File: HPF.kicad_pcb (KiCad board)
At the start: 4 copper layers, 100 x 100 mm, 174 parts, among them J1 CONN_COAXIAL, J2 Conn_01x12, J3 CONN_COAXIAL, J4 CONN_COAXIAL, J5 CONN_COAXIAL, Q2 zvp2106G, U1 AP1117-50, U2 PGA103+

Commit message: new stitching, new gerber
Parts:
- added REF**: via, via:via, F.Cu at (165.0, 111.0)
- added REF**: via, via:via, F.Cu at (156.0, 111.0)
- added REF**: via, via:via, F.Cu at (162.0, 108.0)
- added REF**: via, via:via, F.Cu at (161.0, 108.0)
- added REF**: via, via:via, F.Cu at (160.0, 108.0)
- added REF**: via, via:via, F.Cu at (159.0, 108.0)
- added REF**: via, via:via, F.Cu at (158.0, 108.0)
- added REF**: via, via:via, F.Cu at (157.0, 108.0)
- added REF**: via, via:via, F.Cu at (156.0, 108.0)
- added REF**: via, via:via, F.Cu at (155.0, 108.0)
- added REF**: via, via:via, F.Cu at (154.0, 108.0)
- added REF**: via, via:via, F.Cu at (153.0, 108.0)
- added REF**: via, via:via, F.Cu at (155.0, 111.0)
- added REF**: via, via:via, F.Cu at (152.0, 108.0)
- added REF**: via, via:via, F.Cu at (151.0, 108.0)
- added REF**: via, via:via, F.Cu at (150.0, 108.0)
- added REF**: via, via:via, F.Cu at (149.0, 108.0)
- added REF**: via, via:via, F.Cu at (148.0, 108.0)
- added REF**: via, via:via, F.Cu at (147.0, 108.0)
- added REF**: via, via:via, F.Cu at (146.0, 108.0)
- added REF**: via, via:via, F.Cu at (145.0, 108.0)
- added REF**: via, via:via, F.Cu at (144.0, 108.0)
- added REF**: via, via:via, F.Cu at (143.0, 108.0)
- added REF**: via, via:via, F.Cu at (154.0, 111.0)
- added REF**: via, via:via, F.Cu at (142.0, 108.0)
- added REF**: via, via:via, F.Cu at (141.0, 108.0)
- added REF**: via, via:via, F.Cu at (140.0, 108.0)
- added REF**: via, via:via, F.Cu at (139.0, 108.0)
- added REF**: via, via:via, F.Cu at (138.0, 108.0)
- added REF**: via, via:via, F.Cu at (137.0, 108.0)
- added REF**: via, via:via, F.Cu at (136.0, 108.0)
- added REF**: via, via:via, F.Cu at (135.0, 108.0)
- added REF**: via, via:via, F.Cu at (134.0, 108.0)
- added REF**: via, via:via, F.Cu at (165.0, 107.0)
- added REF**: via, via:via, F.Cu at (153.0, 111.0)
- added REF**: via, via:via, F.Cu at (164.0, 107.0)
- added REF**: via, via:via, F.Cu at (163.0, 107.0)
- added REF**: via, via:via, F.Cu at (162.0, 107.0)
- added REF**: via, via:via, F.Cu at (161.0, 107.0)
- added REF**: via, via:via, F.Cu at (160.0, 107.0)
- added REF**: via, via:via, F.Cu at (159.0, 107.0)
- added REF**: via, via:via, F.Cu at (158.0, 107.0)
- added REF**: via, via:via, F.Cu at (157.0, 107.0)
- added REF**: via, via:via, F.Cu at (156.0, 107.0)
- added REF**: via, via:via, F.Cu at (155.0, 107.0)
- added REF**: via, via:via, F.Cu at (152.0, 111.0)
- added REF**: via, via:via, F.Cu at (154.0, 107.0)
- added REF**: via, via:via, F.Cu at (153.0, 107.0)
- added REF**: via, via:via, F.Cu at (152.0, 107.0)
- added REF**: via, via:via, F.Cu at (151.0, 107.0)
- added REF**: via, via:via, F.Cu at (150.0, 107.0)
- added REF**: via, via:via, F.Cu at (149.0, 107.0)
- added REF**: via, via:via, F.Cu at (148.0, 107.0)
- added REF**: via, via:via, F.Cu at (147.0, 107.0)
- added REF**: via, via:via, F.Cu at (146.0, 107.0)
- added REF**: via, via:via, F.Cu at (145.0, 107.0)
- added REF**: via, via:via, F.Cu at (151.0, 111.0)
- added REF**: via, via:via, F.Cu at (144.0, 107.0)
- added REF**: via, via:via, F.Cu at (143.0, 107.0)
- added REF**: via, via:via, F.Cu at (142.0, 107.0)
- added REF**: via, via:via, F.Cu at (141.0, 107.0)
- added REF**: via, via:via, F.Cu at (140.0, 107.0)
- added REF**: via, via:via, F.Cu at (139.0, 107.0)
- added REF**: via, via:via, F.Cu at (138.0, 107.0)
- added REF**: via, via:via, F.Cu at (137.0, 107.0)
- added REF**: via, via:via, F.Cu at (136.0, 107.0)
- added REF**: via, via:via, F.Cu at (135.0, 107.0)
- added REF**: via, via:via, F.Cu at (150.0, 111.0)
- added REF**: via, via:via, F.Cu at (134.0, 107.0)
- added REF**: via, via:via, F.Cu at (189.0, 103.0)
- added REF**: via, via:via, F.Cu at (189.0, 102.0)
- added REF**: via, via:via, F.Cu at (189.0, 101.0)
- added REF**: via, via:via, F.Cu at (189.0, 100.0)
- added REF**: via, via:via, F.Cu at (189.0, 99.0)
- added REF**: via, via:via, F.Cu at (189.0, 98.0)
- added REF**: via, via:via, F.Cu at (189.0, 97.0)
- added REF**: via, via:via, F.Cu at (189.0, 96.0)
- added REF**: via, via:via, F.Cu at (189.0, 95.0)
- added REF**: via, via:via, F.Cu at (149.0, 111.0)
- added REF**: via, via:via, F.Cu at (189.0, 94.0)
- added REF**: via, via:via, F.Cu at (189.0, 93.0)
- added REF**: via, via:via, F.Cu at (189.0, 92.0)
- added REF**: via, via:via, F.Cu at (189.0, 91.0)
- added REF**: via, via:via, F.Cu at (189.0, 90.0)
- added REF**: via, via:via, F.Cu at (189.0, 89.0)
- added REF**: via, via:via, F.Cu at (189.0, 88.0)
- added REF**: via, via:via, F.Cu at (189.0, 87.0)
- added REF**: via, via:via, F.Cu at (189.0, 86.0)
- added REF**: via, via:via, F.Cu at (189.0, 85.0)
- added REF**: via, via:via, F.Cu at (148.0, 111.0)
- added REF**: via, via:via, F.Cu at (189.0, 84.0)
- added REF**: via, via:via, F.Cu at (189.0, 83.0)
- added REF**: via, via:via, F.Cu at (189.0, 82.0)
- added REF**: via, via:via, F.Cu at (189.0, 81.0)
- added REF**: via, via:via, F.Cu at (189.0, 80.0)
- added REF**: via, via:via, F.Cu at (189.0, 79.0)
- added REF**: via, via:via, F.Cu at (189.0, 78.0)
- added REF**: via, via:via, F.Cu at (189.0, 77.0)
- added REF**: via, via:via, F.Cu at (189.0, 76.0)
- added REF**: via, via:via, F.Cu at (189.0, 75.0)
- added REF**: via, via:via, F.Cu at (147.0, 111.0)
- added REF**: via, via:via, F.Cu at (189.0, 74.0)
- added REF**: via, via:via, F.Cu at (189.0, 73.0)
- added REF**: via, via:via, F.Cu at (189.0, 72.0)
- added REF**: via, via:via, F.Cu at (189.0, 71.0)
- added REF**: via, via:via, F.Cu at (189.0, 70.0)
- added REF**: via, via:via, F.Cu at (189.0, 69.0)
- added REF**: via, via:via, F.Cu at (189.0, 68.0)
- added REF**: via, via:via, F.Cu at (189.0, 67.0)
- added REF**: via, via:via, F.Cu at (189.0, 66.0)
- added REF**: via, via:via, F.Cu at (189.0, 65.0)
- added REF**: via, via:via, F.Cu at (164.0, 111.0)
- added REF**: via, via:via, F.Cu at (146.0, 111.0)
- added REF**: via, via:via, F.Cu at (189.0, 64.0)
- added REF**: via, via:via, F.Cu at (189.0, 63.0)
- added REF**: via, via:via, F.Cu at (189.0, 62.0)
- added REF**: via, via:via, F.Cu at (189.0, 61.0)
- added REF**: via, via:via, F.Cu at (189.0, 60.0)
- added REF**: via, via:via, F.Cu at (189.0, 59.0)
- added REF**: via, via:via, F.Cu at (189.0, 58.0)
- added REF**: via, via:via, F.Cu at (189.0, 57.0)
- added REF**: via, via:via, F.Cu at (189.0, 56.0)
- added REF**: via, via:via, F.Cu at (189.0, 55.0)
- added REF**: via, via:via, F.Cu at (145.0, 111.0)
- added REF**: via, via:via, F.Cu at (189.0, 54.0)
- added REF**: via, via:via, F.Cu at (189.0, 53.0)
- added REF**: via, via:via, F.Cu at (189.0, 52.0)
- added REF**: via, via:via, F.Cu at (189.0, 51.0)
- added REF**: via, via:via, F.Cu at (189.0, 50.0)
- added REF**: via, via:via, F.Cu at (189.0, 49.0)
- added REF**: via, via:via, F.Cu at (189.0, 48.0)
- added REF**: via, via:via, F.Cu at (189.0, 47.0)
- added REF**: via, via:via, F.Cu at (189.0, 46.0)
- added REF**: via, via:via, F.Cu at (189.0, 45.0)
- added REF**: via, via:via, F.Cu at (144.0, 111.0)
- added REF**: via, via:via, F.Cu at (189.0, 44.0)
- added REF**: via, via:via, F.Cu at (189.0, 43.0)
- added REF**: via, via:via, F.Cu at (189.0, 42.0)
- added REF**: via, via:via, F.Cu at (189.0, 41.0)
- added REF**: via, via:via, F.Cu at (189.0, 40.0)
- added REF**: via, via:via, F.Cu at (189.0, 39.0)
- added REF**: via, via:via, F.Cu at (189.0, 38.0)
- added REF**: via, via:via, F.Cu at (189.0, 37.0)
- added REF**: via, via:via, F.Cu at (189.0, 36.0)
- added REF**: via, via:via, F.Cu at (189.0, 35.0)
- added REF**: via, via:via, F.Cu at (143.0, 111.0)
- added REF**: via, via:via, F.Cu at (189.0, 34.0)
- added REF**: via, via:via, F.Cu at (189.0, 33.0)
- added REF**: via, via:via, F.Cu at (189.0, 32.0)
- added REF**: via, via:via, F.Cu at (189.0, 31.0)
- added REF**: via, via:via, F.Cu at (189.0, 30.0)
- added REF**: via, via:via, F.Cu at (189.0, 29.0)
- added REF**: via, via:via, F.Cu at (189.0, 28.0)
- added REF**: via, via:via, F.Cu at (189.0, 27.0)
- added REF**: via, via:via, F.Cu at (189.0, 26.0)
- added REF**: via, via:via, F.Cu at (189.0, 25.0)
- added REF**: via, via:via, F.Cu at (142.0, 111.0)
- added REF**: via, via:via, F.Cu at (189.0, 24.0)
- added REF**: via, via:via, F.Cu at (189.0, 23.0)
- added REF**: via, via:via, F.Cu at (189.0, 22.0)
- added REF**: via, via:via, F.Cu at (189.0, 21.0)
- added REF**: via, via:via, F.Cu at (181.0, 14.0)
- added REF**: via, via:via, F.Cu at (180.0, 14.0)
- added REF**: via, via:via, F.Cu at (179.0, 14.0)
- added REF**: via, via:via, F.Cu at (178.0, 14.0)
- added REF**: via, via:via, F.Cu at (177.0, 14.0)
- added REF**: via, via:via, F.Cu at (176.0, 14.0)
- added REF**: via, via:via, F.Cu at (141.0, 111.0)
- added REF**: via, via:via, F.Cu at (175.0, 14.0)
- added REF**: via, via:via, F.Cu at (174.0, 14.0)
- added REF**: via, via:via, F.Cu at (173.0, 14.0)
- added REF**: via, via:via, F.Cu at (172.0, 14.0)
- added REF**: via, via:via, F.Cu at (171.0, 14.0)
- added REF**: via, via:via, F.Cu at (170.0, 14.0)
- added REF**: via, via:via, F.Cu at (169.0, 14.0)
- added REF**: via, via:via, F.Cu at (168.0, 14.0)
- added REF**: via, via:via, F.Cu at (167.0, 14.0)
- added REF**: via, via:via, F.Cu at (166.0, 14.0)
- added REF**: via, via:via, F.Cu at (140.0, 111.0)
- added REF**: via, via:via, F.Cu at (165.0, 14.0)
- added REF**: via, via:via, F.Cu at (164.0, 14.0)
- added REF**: via, via:via, F.Cu at (163.0, 14.0)
- added REF**: via, via:via, F.Cu at (162.0, 14.0)
- added REF**: via, via:via, F.Cu at (161.0, 14.0)
- added REF**: via, via:via, F.Cu at (160.0, 14.0)
- added REF**: via, via:via, F.Cu at (159.0, 14.0)
- added REF**: via, via:via, F.Cu at (158.0, 14.0)
- added REF**: via, via:via, F.Cu at (157.0, 14.0)
- added REF**: via, via:via, F.Cu at (156.0, 14.0)
- added REF**: via, via:via, F.Cu at (139.0, 111.0)
- added REF**: via, via:via, F.Cu at (155.0, 14.0)
- added REF**: via, via:via, F.Cu at (154.0, 14.0)
- added REF**: via, via:via, F.Cu at (153.0, 14.0)
- added REF**: via, via:via, F.Cu at (152.0, 14.0)
- added REF**: via, via:via, F.Cu at (151.0, 14.0)
- added REF**: via, via:via, F.Cu at (150.0, 14.0)
- added REF**: via, via:via, F.Cu at (149.0, 14.0)
- added REF**: via, via:via, F.Cu at (148.0, 14.0)
- added REF**: via, via:via, F.Cu at (147.0, 14.0)
- added REF**: via, via:via, F.Cu at (146.0, 14.0)
- added REF**: via, via:via, F.Cu at (138.0, 111.0)
- added REF**: via, via:via, F.Cu at (145.0, 14.0)
- added REF**: via, via:via, F.Cu at (144.0, 14.0)
- added REF**: via, via:via, F.Cu at (143.0, 14.0)
- added REF**: via, via:via, F.Cu at (142.0, 14.0)
- added REF**: via, via:via, F.Cu at (141.0, 14.0)
- added REF**: via, via:via, F.Cu at (140.0, 14.0)
- added REF**: via, via:via, F.Cu at (139.0, 14.0)
- added REF**: via, via:via, F.Cu at (138.0, 14.0)
- added REF**: via, via:via, F.Cu at (137.0, 14.0)
- added REF**: via, via:via, F.Cu at (136.0, 14.0)
- added REF**: via, via:via, F.Cu at (137.0, 111.0)
- added REF**: via, via:via, F.Cu at (135.0, 14.0)
- added REF**: via, via:via, F.Cu at (134.0, 14.0)
- added REF**: via, via:via, F.Cu at (133.0, 14.0)
- added REF**: via, via:via, F.Cu at (132.0, 14.0)
- added REF**: via, via:via, F.Cu at (131.0, 14.0)
- added REF**: via, via:via, F.Cu at (130.0, 14.0)
- added REF**: via, via:via, F.Cu at (129.0, 14.0)
- added REF**: via, via:via, F.Cu at (128.0, 14.0)
- added REF**: via, via:via, F.Cu at (127.0, 14.0)
- added REF**: via, via:via, F.Cu at (126.0, 14.0)
- added REF**: via, via:via, F.Cu at (163.0, 111.0)
- added REF**: via, via:via, F.Cu at (136.0, 111.0)
- added REF**: via, via:via, F.Cu at (125.0, 14.0)
- added REF**: via, via:via, F.Cu at (124.0, 14.0)
- added REF**: via, via:via, F.Cu at (123.0, 14.0)
- added REF**: via, via:via, F.Cu at (122.0, 14.0)
- added REF**: via, via:via, F.Cu at (121.0, 14.0)
- added REF**: via, via:via, F.Cu at (120.0, 14.0)
- added REF**: via, via:via, F.Cu at (119.0, 14.0)
- added REF**: via, via:via, F.Cu at (118.0, 14.0)
- added REF**: via, via:via, F.Cu at (117.0, 14.0)
- added REF**: via, via:via, F.Cu at (116.0, 14.0)
- added REF**: via, via:via, F.Cu at (135.0, 111.0)
- added REF**: via, via:via, F.Cu at (115.0, 14.0)
- added REF**: via, via:via, F.Cu at (114.0, 14.0)
- added REF**: via, via:via, F.Cu at (113.0, 14.0)
- added REF**: via, via:via, F.Cu at (112.0, 14.0)
- added REF**: via, via:via, F.Cu at (111.0, 14.0)
- added REF**: via, via:via, F.Cu at (110.0, 14.0)
- added REF**: via, via:via, F.Cu at (109.0, 14.0)
- added REF**: via, via:via, F.Cu at (108.0, 14.0)
- added REF**: via, via:via, F.Cu at (107.0, 14.0)
- added REF**: via, via:via, F.Cu at (106.0, 14.0)
- added REF**: via, via:via, F.Cu at (134.0, 111.0)
- added REF**: via, via:via, F.Cu at (105.0, 14.0)
- added REF**: via, via:via, F.Cu at (104.0, 14.0)
- added REF**: via, via:via, F.Cu at (103.0, 14.0)
- added REF**: via, via:via, F.Cu at (102.0, 14.0)
- added REF**: via, via:via, F.Cu at (101.0, 14.0)
- added REF**: via, via:via, F.Cu at (100.0, 14.0)
- added REF**: via, via:via, F.Cu at (94.0, 103.0)
- added REF**: via, via:via, F.Cu at (93.0, 103.0)
- added REF**: via, via:via, F.Cu at (92.0, 103.0)
- added REF**: via, via:via, F.Cu at (91.0, 103.0)
- added REF**: via, via:via, F.Cu at (165.0, 110.0)
- added REF**: via, via:via, F.Cu at (94.0, 102.0)
- added REF**: via, via:via, F.Cu at (93.0, 102.0)
- added REF**: via, via:via, F.Cu at (92.0, 102.0)
- added REF**: via, via:via, F.Cu at (91.0, 102.0)
- added REF**: via, via:via, F.Cu at (94.0, 101.0)
- added REF**: via, via:via, F.Cu at (93.0, 101.0)
- added REF**: via, via:via, F.Cu at (92.0, 101.0)
- added REF**: via, via:via, F.Cu at (91.0, 101.0)
- added REF**: via, via:via, F.Cu at (94.0, 100.0)
- added REF**: via, via:via, F.Cu at (93.0, 100.0)
- added REF**: via, via:via, F.Cu at (164.0, 110.0)
- added REF**: via, via:via, F.Cu at (92.0, 100.0)
- added REF**: via, via:via, F.Cu at (91.0, 100.0)
- added REF**: via, via:via, F.Cu at (94.0, 99.0)
- added REF**: via, via:via, F.Cu at (93.0, 99.0)
- added REF**: via, via:via, F.Cu at (92.0, 99.0)
- added REF**: via, via:via, F.Cu at (91.0, 99.0)
- added REF**: via, via:via, F.Cu at (94.0, 98.0)
- added REF**: via, via:via, F.Cu at (93.0, 98.0)
- added REF**: via, via:via, F.Cu at (92.0, 98.0)
- added REF**: via, via:via, F.Cu at (91.0, 98.0)
- added REF**: via, via:via, F.Cu at (163.0, 110.0)
- added REF**: via, via:via, F.Cu at (94.0, 97.0)
- added REF**: via, via:via, F.Cu at (93.0, 97.0)
- added REF**: via, via:via, F.Cu at (92.0, 97.0)
- added REF**: via, via:via, F.Cu at (91.0, 97.0)
- added REF**: via, via:via, F.Cu at (94.0, 96.0)
- added REF**: via, via:via, F.Cu at (93.0, 96.0)
- added REF**: via, via:via, F.Cu at (92.0, 96.0)
- added REF**: via, via:via, F.Cu at (91.0, 96.0)
- added REF**: via, via:via, F.Cu at (94.0, 95.0)
- added REF**: via, via:via, F.Cu at (93.0, 95.0)
- added REF**: via, via:via, F.Cu at (162.0, 110.0)
- added REF**: via, via:via, F.Cu at (92.0, 95.0)
- added REF**: via, via:via, F.Cu at (91.0, 95.0)
- added REF**: via, via:via, F.Cu at (94.0, 94.0)
- added REF**: via, via:via, F.Cu at (93.0, 94.0)
- added REF**: via, via:via, F.Cu at (92.0, 94.0)
- added REF**: via, via:via, F.Cu at (91.0, 94.0)
- added REF**: via, via:via, F.Cu at (94.0, 93.0)
- added REF**: via, via:via, F.Cu at (93.0, 93.0)
- added REF**: via, via:via, F.Cu at (92.0, 93.0)
- added REF**: via, via:via, F.Cu at (91.0, 93.0)
- added REF**: via, via:via, F.Cu at (161.0, 110.0)
- added REF**: via, via:via, F.Cu at (94.0, 92.0)
- added REF**: via, via:via, F.Cu at (93.0, 92.0)
- added REF**: via, via:via, F.Cu at (92.0, 92.0)
- added REF**: via, via:via, F.Cu at (91.0, 92.0)
- added REF**: via, via:via, F.Cu at (94.0, 91.0)
- added REF**: via, via:via, F.Cu at (93.0, 91.0)
- added REF**: via, via:via, F.Cu at (92.0, 91.0)
- added REF**: via, via:via, F.Cu at (91.0, 91.0)
- added REF**: via, via:via, F.Cu at (94.0, 90.0)
- added REF**: via, via:via, F.Cu at (93.0, 90.0)
- added REF**: via, via:via, F.Cu at (160.0, 110.0)
- added REF**: via, via:via, F.Cu at (92.0, 90.0)
- added REF**: via, via:via, F.Cu at (91.0, 90.0)
- added REF**: via, via:via, F.Cu at (94.0, 89.0)
- added REF**: via, via:via, F.Cu at (93.0, 89.0)
- added REF**: via, via:via, F.Cu at (92.0, 89.0)
- added REF**: via, via:via, F.Cu at (91.0, 89.0)
- added REF**: via, via:via, F.Cu at (94.0, 88.0)
- added REF**: via, via:via, F.Cu at (93.0, 88.0)
- added REF**: via, via:via, F.Cu at (92.0, 88.0)
- added REF**: via, via:via, F.Cu at (91.0, 88.0)
- added REF**: via, via:via, F.Cu at (159.0, 110.0)
- added REF**: via, via:via, F.Cu at (94.0, 87.0)
- added REF**: via, via:via, F.Cu at (93.0, 87.0)
- added REF**: via, via:via, F.Cu at (92.0, 87.0)
- added REF**: via, via:via, F.Cu at (91.0, 87.0)
- added REF**: via, via:via, F.Cu at (94.0, 86.0)
- added REF**: via, via:via, F.Cu at (93.0, 86.0)
- added REF**: via, via:via, F.Cu at (92.0, 86.0)
- added REF**: via, via:via, F.Cu at (91.0, 86.0)
- added REF**: via, via:via, F.Cu at (94.0, 85.0)
- added REF**: via, via:via, F.Cu at (93.0, 85.0)
- added REF**: via, via:via, F.Cu at (162.0, 111.0)
- added REF**: via, via:via, F.Cu at (158.0, 110.0)
- added REF**: via, via:via, F.Cu at (92.0, 85.0)
- added REF**: via, via:via, F.Cu at (91.0, 85.0)
- added REF**: via, via:via, F.Cu at (94.0, 84.0)
- added REF**: via, via:via, F.Cu at (93.0, 84.0)
- added REF**: via, via:via, F.Cu at (92.0, 84.0)
- added REF**: via, via:via, F.Cu at (91.0, 84.0)
- added REF**: via, via:via, F.Cu at (94.0, 83.0)
- added REF**: via, via:via, F.Cu at (93.0, 83.0)
- added REF**: via, via:via, F.Cu at (92.0, 83.0)
- added REF**: via, via:via, F.Cu at (91.0, 83.0)
- added REF**: via, via:via, F.Cu at (157.0, 110.0)
- added REF**: via, via:via, F.Cu at (94.0, 82.0)
- added REF**: via, via:via, F.Cu at (93.0, 82.0)
- added REF**: via, via:via, F.Cu at (92.0, 82.0)
- added REF**: via, via:via, F.Cu at (91.0, 82.0)
- added REF**: via, via:via, F.Cu at (94.0, 81.0)
- added REF**: via, via:via, F.Cu at (93.0, 81.0)
- added REF**: via, via:via, F.Cu at (92.0, 81.0)
- added REF**: via, via:via, F.Cu at (91.0, 81.0)
- added REF**: via, via:via, F.Cu at (94.0, 80.0)
- added REF**: via, via:via, F.Cu at (93.0, 80.0)
- added REF**: via, via:via, F.Cu at (156.0, 110.0)
- added REF**: via, via:via, F.Cu at (92.0, 80.0)
- added REF**: via, via:via, F.Cu at (91.0, 80.0)
- added REF**: via, via:via, F.Cu at (94.0, 79.0)
- added REF**: via, via:via, F.Cu at (93.0, 79.0)
- added REF**: via, via:via, F.Cu at (92.0, 79.0)
- added REF**: via, via:via, F.Cu at (91.0, 79.0)
- added REF**: via, via:via, F.Cu at (94.0, 78.0)
- added REF**: via, via:via, F.Cu at (93.0, 78.0)
- added REF**: via, via:via, F.Cu at (92.0, 78.0)
- added REF**: via, via:via, F.Cu at (91.0, 78.0)
- added REF**: via, via:via, F.Cu at (155.0, 110.0)
- added REF**: via, via:via, F.Cu at (94.0, 77.0)
- added REF**: via, via:via, F.Cu at (93.0, 77.0)
- added REF**: via, via:via, F.Cu at (92.0, 77.0)
- added REF**: via, via:via, F.Cu at (91.0, 77.0)
- added REF**: via, via:via, F.Cu at (94.0, 76.0)
- added REF**: via, via:via, F.Cu at (93.0, 76.0)
- added REF**: via, via:via, F.Cu at (92.0, 76.0)
- added REF**: via, via:via, F.Cu at (91.0, 76.0)
- added REF**: via, via:via, F.Cu at (94.0, 75.0)
- added REF**: via, via:via, F.Cu at (93.0, 75.0)
- added REF**: via, via:via, F.Cu at (154.0, 110.0)
- added REF**: via, via:via, F.Cu at (92.0, 75.0)
- added REF**: via, via:via, F.Cu at (91.0, 75.0)
- added REF**: via, via:via, F.Cu at (94.0, 74.0)
- added REF**: via, via:via, F.Cu at (93.0, 74.0)
- added REF**: via, via:via, F.Cu at (92.0, 74.0)
- added REF**: via, via:via, F.Cu at (91.0, 74.0)
- added REF**: via, via:via, F.Cu at (94.0, 73.0)
- added REF**: via, via:via, F.Cu at (93.0, 73.0)
- added REF**: via, via:via, F.Cu at (92.0, 73.0)
- added REF**: via, via:via, F.Cu at (91.0, 73.0)
- added REF**: via, via:via, F.Cu at (153.0, 110.0)
- added REF**: via, via:via, F.Cu at (94.0, 72.0)
- added REF**: via, via:via, F.Cu at (93.0, 72.0)
- added REF**: via, via:via, F.Cu at (92.0, 72.0)
- added REF**: via, via:via, F.Cu at (91.0, 72.0)
- added REF**: via, via:via, F.Cu at (94.0, 71.0)
- added REF**: via, via:via, F.Cu at (93.0, 71.0)
- added REF**: via, via:via, F.Cu at (92.0, 71.0)
- added REF**: via, via:via, F.Cu at (91.0, 71.0)
- added REF**: via, via:via, F.Cu at (94.0, 70.0)
- added REF**: via, via:via, F.Cu at (93.0, 70.0)
- added REF**: via, via:via, F.Cu at (152.0, 110.0)
- added REF**: via, via:via, F.Cu at (92.0, 70.0)
- added REF**: via, via:via, F.Cu at (91.0, 70.0)
- added REF**: via, via:via, F.Cu at (94.0, 69.0)
- added REF**: via, via:via, F.Cu at (93.0, 69.0)
- added REF**: via, via:via, F.Cu at (92.0, 69.0)
- added REF**: via, via:via, F.Cu at (91.0, 69.0)
- added REF**: via, via:via, F.Cu at (94.0, 68.0)
- added REF**: via, via:via, F.Cu at (93.0, 68.0)
- added REF**: via, via:via, F.Cu at (92.0, 68.0)
- added REF**: via, via:via, F.Cu at (91.0, 68.0)
- added REF**: via, via:via, F.Cu at (151.0, 110.0)
- added REF**: via, via:via, F.Cu at (94.0, 67.0)
- added REF**: via, via:via, F.Cu at (93.0, 67.0)
- added REF**: via, via:via, F.Cu at (92.0, 67.0)
- added REF**: via, via:via, F.Cu at (91.0, 67.0)
- added REF**: via, via:via, F.Cu at (94.0, 66.0)
- added REF**: via, via:via, F.Cu at (93.0, 66.0)
- added REF**: via, via:via, F.Cu at (92.0, 66.0)
- added REF**: via, via:via, F.Cu at (91.0, 66.0)
- added REF**: via, via:via, F.Cu at (94.0, 65.0)
- added REF**: via, via:via, F.Cu at (93.0, 65.0)
- added REF**: via, via:via, F.Cu at (150.0, 110.0)
- added REF**: via, via:via, F.Cu at (92.0, 65.0)
- added REF**: via, via:via, F.Cu at (91.0, 65.0)
- added REF**: via, via:via, F.Cu at (94.0, 64.0)
- added REF**: via, via:via, F.Cu at (93.0, 64.0)
- added REF**: via, via:via, F.Cu at (92.0, 64.0)
- added REF**: via, via:via, F.Cu at (91.0, 64.0)
- added REF**: via, via:via, F.Cu at (94.0, 63.0)
- added REF**: via, via:via, F.Cu at (93.0, 63.0)
- added REF**: via, via:via, F.Cu at (92.0, 63.0)
- added REF**: via, via:via, F.Cu at (91.0, 63.0)
- added REF**: via, via:via, F.Cu at (149.0, 110.0)
- added REF**: via, via:via, F.Cu at (94.0, 62.0)
- added REF**: via, via:via, F.Cu at (93.0, 62.0)
- added REF**: via, via:via, F.Cu at (92.0, 62.0)
- added REF**: via, via:via, F.Cu at (91.0, 62.0)
- added REF**: via, via:via, F.Cu at (94.0, 61.0)
- added REF**: via, via:via, F.Cu at (93.0, 61.0)
- added REF**: via, via:via, F.Cu at (92.0, 61.0)
- added REF**: via, via:via, F.Cu at (91.0, 61.0)
- added REF**: via, via:via, F.Cu at (94.0, 60.0)
- added REF**: via, via:via, F.Cu at (93.0, 60.0)
- added REF**: via, via:via, F.Cu at (161.0, 111.0)
- added REF**: via, via:via, F.Cu at (148.0, 110.0)
- added REF**: via, via:via, F.Cu at (92.0, 60.0)
- added REF**: via, via:via, F.Cu at (91.0, 60.0)
- added REF**: via, via:via, F.Cu at (94.0, 59.0)
- added REF**: via, via:via, F.Cu at (93.0, 59.0)
- added REF**: via, via:via, F.Cu at (92.0, 59.0)
- added REF**: via, via:via, F.Cu at (91.0, 59.0)
- added REF**: via, via:via, F.Cu at (94.0, 58.0)
- added REF**: via, via:via, F.Cu at (93.0, 58.0)
- added REF**: via, via:via, F.Cu at (92.0, 58.0)
- added REF**: via, via:via, F.Cu at (91.0, 58.0)
- added REF**: via, via:via, F.Cu at (147.0, 110.0)
- added REF**: via, via:via, F.Cu at (94.0, 57.0)
- added REF**: via, via:via, F.Cu at (93.0, 57.0)
- added REF**: via, via:via, F.Cu at (92.0, 57.0)
- added REF**: via, via:via, F.Cu at (91.0, 57.0)
- added REF**: via, via:via, F.Cu at (94.0, 56.0)
- added REF**: via, via:via, F.Cu at (93.0, 56.0)
- added REF**: via, via:via, F.Cu at (92.0, 56.0)
- added REF**: via, via:via, F.Cu at (91.0, 56.0)
- added REF**: via, via:via, F.Cu at (94.0, 55.0)
- added REF**: via, via:via, F.Cu at (93.0, 55.0)
- added REF**: via, via:via, F.Cu at (146.0, 110.0)
- added REF**: via, via:via, F.Cu at (92.0, 55.0)
- added REF**: via, via:via, F.Cu at (91.0, 55.0)
- added REF**: via, via:via, F.Cu at (94.0, 54.0)
- added REF**: via, via:via, F.Cu at (93.0, 54.0)
- added REF**: via, via:via, F.Cu at (92.0, 54.0)
- added REF**: via, via:via, F.Cu at (91.0, 54.0)
- added REF**: via, via:via, F.Cu at (94.0, 53.0)
- added REF**: via, via:via, F.Cu at (93.0, 53.0)
- added REF**: via, via:via, F.Cu at (92.0, 53.0)
- added REF**: via, via:via, F.Cu at (91.0, 53.0)
- added REF**: via, via:via, F.Cu at (145.0, 110.0)
- added REF**: via, via:via, F.Cu at (94.0, 52.0)
- added REF**: via, via:via, F.Cu at (93.0, 52.0)
- added REF**: via, via:via, F.Cu at (92.0, 52.0)
- added REF**: via, via:via, F.Cu at (91.0, 52.0)
- added REF**: via, via:via, F.Cu at (94.0, 51.0)
- added REF**: via, via:via, F.Cu at (93.0, 51.0)
- added REF**: via, via:via, F.Cu at (92.0, 51.0)
- added REF**: via, via:via, F.Cu at (91.0, 51.0)
- added REF**: via, via:via, F.Cu at (94.0, 50.0)
- added REF**: via, via:via, F.Cu at (93.0, 50.0)
- added REF**: via, via:via, F.Cu at (144.0, 110.0)
- added REF**: via, via:via, F.Cu at (92.0, 50.0)
- added REF**: via, via:via, F.Cu at (91.0, 50.0)
- added REF**: via, via:via, F.Cu at (94.0, 49.0)
- added REF**: via, via:via, F.Cu at (93.0, 49.0)
- added REF**: via, via:via, F.Cu at (92.0, 49.0)
- added REF**: via, via:via, F.Cu at (91.0, 49.0)
- added REF**: via, via:via, F.Cu at (94.0, 48.0)
- added REF**: via, via:via, F.Cu at (93.0, 48.0)
- added REF**: via, via:via, F.Cu at (92.0, 48.0)
- added REF**: via, via:via, F.Cu at (91.0, 48.0)
- added REF**: via, via:via, F.Cu at (143.0, 110.0)
- added REF**: via, via:via, F.Cu at (94.0, 47.0)
- added REF**: via, via:via, F.Cu at (93.0, 47.0)
- added REF**: via, via:via, F.Cu at (92.0, 47.0)
- added REF**: via, via:via, F.Cu at (91.0, 47.0)
- added REF**: via, via:via, F.Cu at (94.0, 46.0)
- added REF**: via, via:via, F.Cu at (93.0, 46.0)
- added REF**: via, via:via, F.Cu at (92.0, 46.0)
- added REF**: via, via:via, F.Cu at (91.0, 46.0)
- added REF**: via, via:via, F.Cu at (94.0, 45.0)
- added REF**: via, via:via, F.Cu at (93.0, 45.0)
- added REF**: via, via:via, F.Cu at (142.0, 110.0)
- added REF**: via, via:via, F.Cu at (92.0, 45.0)
- added REF**: via, via:via, F.Cu at (91.0, 45.0)
- added REF**: via, via:via, F.Cu at (94.0, 44.0)
- added REF**: via, via:via, F.Cu at (93.0, 44.0)
- added REF**: via, via:via, F.Cu at (92.0, 44.0)
- added REF**: via, via:via, F.Cu at (91.0, 44.0)
- added REF**: via, via:via, F.Cu at (94.0, 43.0)
- added REF**: via, via:via, F.Cu at (93.0, 43.0)
- added REF**: via, via:via, F.Cu at (92.0, 43.0)
- added REF**: via, via:via, F.Cu at (91.0, 43.0)
- added REF**: via, via:via, F.Cu at (141.0, 110.0)
- added REF**: via, via:via, F.Cu at (94.0, 42.0)
- added REF**: via, via:via, F.Cu at (93.0, 42.0)
- added REF**: via, via:via, F.Cu at (92.0, 42.0)
- added REF**: via, via:via, F.Cu at (91.0, 42.0)
- added REF**: via, via:via, F.Cu at (94.0, 41.0)
- added REF**: via, via:via, F.Cu at (93.0, 41.0)
- added REF**: via, via:via, F.Cu at (92.0, 41.0)
- added REF**: via, via:via, F.Cu at (91.0, 41.0)
- added REF**: via, via:via, F.Cu at (94.0, 40.0)
- added REF**: via, via:via, F.Cu at (93.0, 40.0)
- added REF**: via, via:via, F.Cu at (140.0, 110.0)
- added REF**: via, via:via, F.Cu at (92.0, 40.0)
- added REF**: via, via:via, F.Cu at (91.0, 40.0)
- added REF**: via, via:via, F.Cu at (94.0, 39.0)
- added REF**: via, via:via, F.Cu at (93.0, 39.0)
- added REF**: via, via:via, F.Cu at (92.0, 39.0)
- added REF**: via, via:via, F.Cu at (91.0, 39.0)
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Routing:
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
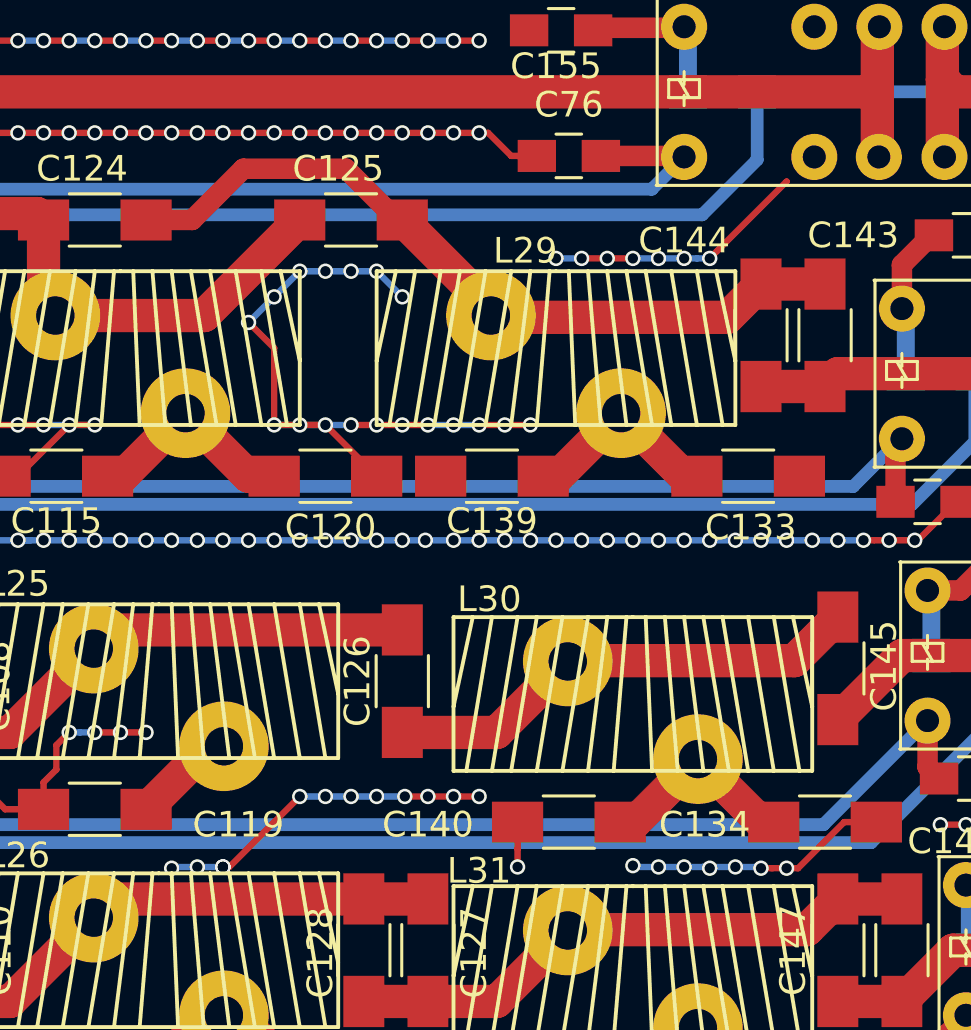
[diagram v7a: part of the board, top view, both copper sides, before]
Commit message: silkmask mods,, gnd stitching cleaning, gerber added
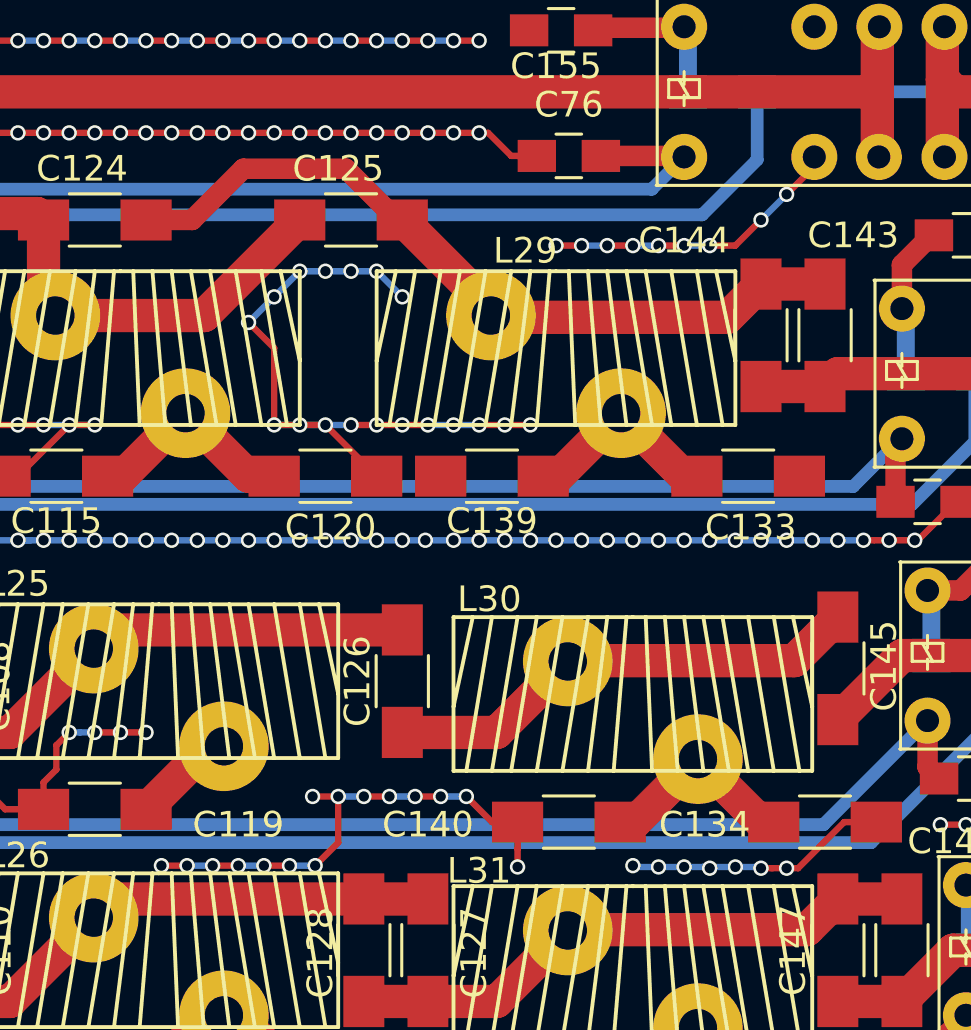
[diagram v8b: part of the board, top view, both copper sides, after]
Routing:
- net GND: track 827.8 -> 857.0 mm, vias 454 -> 477
- net (no net): track 23.7 -> 0.00 mm, vias 19 -> 0
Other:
- board text added: "1.5 MHz"
- board text added: "13 Mhz"
- board text added: "20 Mhz"
- board text added: "50-54 MHz/LNA"
- board text added: "6.5 Mhz"
- board text added: "9.5 Mhz"
- board text added: "By-Pass"
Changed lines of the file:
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@@
     (links 1030)
     (no_connects 0)
-    (area 89.157143 12.025 191.842858 121.775001)
+    (area 89.924999 12.424999 190.075001 112.575001)
     (thickness 1.6)
-    (drawings 16)
-    (tracks 1845)
+    (drawings 23)
+    (tracks 1852)
     (zones 0)
     (modules 827)
@@
       (net 2 GND) (zone_connect 2))
   )
+  (gr_text "50-54 MHz/LNA" (at 153 85) (layer B.SilkS)
+    (effects (font (size 1.5 1.5) (thickness 0.3)) (justify mirror))
+  )
+  (gr_text "20 Mhz" (at 148 73) (layer B.SilkS)
+    (effects (font (size 1.5 1.5) (thickness 0.3)) (justify mirror))
+  )
+  (gr_text "13 Mhz" (at 148 62) (layer B.SilkS)
+    (effects (font (size 1.5 1.5) (thickness 0.3)) (justify mirror))
+  )
+  (gr_text "9.5 Mhz\n" (at 148 51) (layer B.SilkS)
+    (effects (font (size 1.5 1.5) (thickness 0.3)) (justify mirror))
+  )
+  (gr_text "6.5 Mhz" (at 148 41) (layer B.SilkS)
+    (effects (font (size 1.5 1.5) (thickness 0.3)) (justify mirror))
+  )
+  (gr_text "1.5 MHz" (at 147 28) (layer B.SilkS)
+    (effects (font (size 1.5 1.5) (thickness 0.3)) (justify mirror))
+  )
+  (gr_text By-Pass (at 142 19) (layer B.SilkS)
+    (effects (font (size 1.5 1.5) (thickness 0.3)) (justify mirror))
+  )
   (gr_text "From RX LPF" (at 129.5 100.5) (layer F.SilkS)
     (effects (font (size 1.5 1.5) (thickness 0.3)))
@@
   (gr_line (start 90 12.5) (end 190 12.5) (angle 90) (layer Edge.Cuts) (width 0.15))
   (gr_line (start 90 112.5) (end 90 12.5) (angle 90) (layer Edge.Cuts) (width 0.15))
-  (segment (start 162 25.5) (end 162.5 25.5) (width 0.25) (layer B.Cu) (net 0))
-  (via (at 162 25.5) (size 0.6) (drill 0.4) (layers F.Cu B.Cu) (net 0))
-  (segment (start 161 25.5) (end 162 25.5) (width 0.25) (layer B.Cu) (net 0))
-  (segment (start 166 22.500004) (end 163.300003 25.200001) (width 0.25) (layer F.Cu) (net 0))
-  (segment (start 166 22.5) (end 166 22.500004) (width 0.25) (layer F.Cu) (net 0))
-  (segment (start 162.5 25.5) (end 163.000004 25.5) (width 0.25) (layer B.Cu) (net 0))
-  (segment (start 163.300003 25.200001) (end 163.000004 25.5) (width 0.25) (layer F.Cu) (net 0))
-  (via (at 163.000004 25.5) (size 0.6) (drill 0.4) (layers F.Cu B.Cu) (net 0))
-  (segment (start 161 25.5) (end 160 25.5) (width 0.25) (layer B.Cu) (net 0))
-  (via (at 161 25.5) (size 0.6) (drill 0.4) (layers F.Cu B.Cu) (net 0))
-  (segment (start 159 25.5) (end 160 25.5) (width 0.25) (layer F.Cu) (net 0))
-  (via (at 160 25.5) (size 0.6) (drill 0.4) (layers F.Cu B.Cu) (net 0))
-  (segment (start 158 25.5) (end 157 25.5) (width 0.25) (layer B.Cu) (net 0))
-  (via (at 157 25.5) (size 0.6) (drill 0.4) (layers F.Cu B.Cu) (net 0))
-  (segment (start 159 25.5) (end 158 25.5) (width 0.25) (layer F.Cu) (net 0))
-  (via (at 159 25.5) (size 0.6) (drill 0.4) (layers F.Cu B.Cu) (net 0))
-  (via (at 158 25.5) (size 0.6) (drill 0.4) (layers F.Cu B.Cu) (net 0))
-  (segment (start 154 46.5) (end 153 46.5) (width 0.25) (layer F.Cu) (net 0))
-  (segment (start 152 46.5) (end 153 46.5) (width 0.25) (layer F.Cu) (net 0))
-  (segment (start 153.25 46.5) (end 153 46.5) (width 0.25) (layer F.Cu) (net 0))
-  (via (at 153 46.5) (size 0.6) (drill 0.4) (layers F.Cu B.Cu) (net 0))
-  (via (at 154 46.5) (size 0.6) (drill 0.4) (layers F.Cu B.Cu) (net 0))
-  (segment (start 152 46.5) (end 151.1 46.5) (width 0.25) (layer F.Cu) (net 0))
-  (via (at 152 46.5) (size 0.6) (drill 0.4) (layers F.Cu B.Cu) (net 0))
-  (segment (start 150 46.5) (end 151.1 46.5) (width 0.25) (layer B.Cu) (net 0))
-  (via (at 151.1 46.5) (size 0.6) (drill 0.4) (layers F.Cu B.Cu) (net 0))
-  (segment (start 150 46.5) (end 149 46.5) (width 0.25) (layer B.Cu) (net 0))
-  (via (at 150 46.5) (size 0.6) (drill 0.4) (layers F.Cu B.Cu) (net 0))
-  (segment (start 148 46.5) (end 147.000004 46.5) (width 0.25) (layer B.Cu) (net 0))
-  (segment (start 149 46.5) (end 148 46.5) (width 0.25) (layer B.Cu) (net 0))
-  (via (at 148 46.5) (size 0.6) (drill 0.4) (layers F.Cu B.Cu) (net 0))
-  (segment (start 144 49.25) (end 144.25 49.25) (width 0.25) (layer F.Cu) (net 0))
-  (segment (start 144.25 49.25) (end 147 46.5) (width 0.25) (layer F.Cu) (net 0))
-  (segment (start 147 46.5) (end 147.000004 46.5) (width 0.25) (layer F.Cu) (net 0))
-  (via (at 147.000004 46.5) (size 0.6) (drill 0.4) (layers F.Cu B.Cu) (net 0))
-  (segment (start 143 49.25) (end 142.05 49.25) (width 0.25) (layer B.Cu) (net 0))
-  (segment (start 144 49.25) (end 143 49.25) (width 0.25) (layer B.Cu) (net 0))
-  (via (at 143 49.25) (size 0.6) (drill 0.4) (layers F.Cu B.Cu) (net 0))
-  (segment (start 142.05 49.25) (end 142 49.3) (width 0.25) (layer B.Cu) (net 0))
-  (via (at 142 49.3) (size 0.6) (drill 0.4) (layers F.Cu B.Cu) (net 0))
-  (via (at 144 49.25) (size 0.6) (drill 0.4) (layers F.Cu B.Cu) (net 0))
-  (via (at 144 49.25) (size 0.6) (drill 0.4) (layers F.Cu B.Cu) (net 0))
-  (via (at 149 46.5) (size 0.6) (drill 0.4) (layers F.Cu B.Cu) (net 0))
   (segment (start 168.360031 65.54) (end 164.950044 68.949987) (width 0.5) (layer B.Cu) (net 1))
   (segment (start 164.950044 68.949987) (end 145.760048 68.949987) (width 0.5) (layer B.Cu) (net 1))
@@
   (segment (start 168.24 91.8) (end 172.100001 87.939999) (width 0.8) (layer B.Cu) (net 1))
   (segment (start 134 91.8) (end 168.24 91.8) (width 0.8) (layer B.Cu) (net 1))
+  (segment (start 148.5 46.5) (end 148.5 48.3) (width 0.25) (layer F.Cu) (net 2))
+  (via (at 141.6 49.2) (size 0.6) (drill 0.4) (layers F.Cu B.Cu) (net 2))
+  (segment (start 142.6 49.2) (end 141.6 49.2) (width 0.25) (layer F.Cu) (net 2))
+  (via (at 142.6 49.2) (size 0.6) (drill 0.4) (layers F.Cu B.Cu) (net 2))
+  (segment (start 143.6 49.2) (end 142.6 49.2) (width 0.25) (layer B.Cu) (net 2))
+  (via (at 143.6 49.2) (size 0.6) (drill 0.4) (layers F.Cu B.Cu) (net 2))
+  (segment (start 144.6 49.2) (end 143.6 49.2) (width 0.25) (layer F.Cu) (net 2))
+  (via (at 144.6 49.2) (size 0.6) (drill 0.4) (layers F.Cu B.Cu) (net 2))
+  (segment (start 145.6 49.2) (end 144.6 49.2) (width 0.25) (layer B.Cu) (net 2))
+  (via (at 145.6 49.2) (size 0.6) (drill 0.4) (layers F.Cu B.Cu) (net 2))
+  (segment (start 146.6 49.2) (end 145.6 49.2) (width 0.25) (layer F.Cu) (net 2))
+  (via (at 146.6 49.2) (size 0.6) (drill 0.4) (layers F.Cu B.Cu) (net 2))
+  (segment (start 147.6 49.2) (end 146.6 49.2) (width 0.25) (layer B.Cu) (net 2))
+  (via (at 147.6 49.2) (size 0.6) (drill 0.4) (layers F.Cu B.Cu) (net 2))
+  (segment (start 148.5 48.3) (end 147.6 49.2) (width 0.25) (layer F.Cu) (net 2))
+  (segment (start 153.5 46.5) (end 152.5 46.5) (width 0.25) (layer B.Cu) (net 2))
+  (via (at 153.5 46.5) (size 0.6) (drill 0.4) (layers F.Cu B.Cu) (net 2))
+  (segment (start 154.5 47.5) (end 153.5 46.5) (width 0.25) (layer F.Cu) (net 2) (status 400000))
+  (via (at 147.5 46.5) (size 0.6) (drill 0.4) (layers F.Cu B.Cu) (net 2))
+  (segment (start 148.5 46.5) (end 147.5 46.5) (width 0.25) (layer F.Cu) (net 2))
+  (via (at 148.5 46.5) (size 0.6) (drill 0.4) (layers F.Cu B.Cu) (net 2))
+  (segment (start 149.5 46.5) (end 148.5 46.5) (width 0.25) (layer B.Cu) (net 2))
+  (via (at 149.5 46.5) (size 0.6) (drill 0.4) (layers F.Cu B.Cu) (net 2))
+  (segment (start 150.5 46.5) (end 149.5 46.5) (width 0.25) (layer F.Cu) (net 2))
+  (via (at 150.5 46.5) (size 0.6) (drill 0.4) (layers F.Cu B.Cu) (net 2))
+  (segment (start 151.5 46.5) (end 150.5 46.5) (width 0.25) (layer B.Cu) (net 2))
+  (via (at 151.5 46.5) (size 0.6) (drill 0.4) (layers F.Cu B.Cu) (net 2))
+  (segment (start 152.5 46.5) (end 151.5 46.5) (width 0.25) (layer F.Cu) (net 2))
+  (via (at 152.5 46.5) (size 0.6) (drill 0.4) (layers F.Cu B.Cu) (net 2))
+  (segment (start 155.5 47.5) (end 154.5 47.5) (width 0.25) (layer F.Cu) (net 2) (status C00000))
+  (segment (start 167.08 21.54) (end 167.08 21.92) (width 0.25) (layer F.Cu) (net 2) (status C00000))
+  (segment (start 167.08 21.92) (end 166 23) (width 0.25) (layer F.Cu) (net 2) (status 400000))
+  (via (at 166 23) (size 0.6) (drill 0.4) (layers F.Cu B.Cu) (net 2))
+  (segment (start 166 23) (end 165 24) (width 0.25) (layer B.Cu) (net 2))
+  (via (at 165 24) (size 0.6) (drill 0.4) (layers F.Cu B.Cu) (net 2))
+  (segment (start 165 24) (end 164 25) (width 0.25) (layer F.Cu) (net 2))
+  (segment (start 164 25) (end 163 25) (width 0.25) (layer F.Cu) (net 2))
+  (via (at 163 25) (size 0.6) (drill 0.4) (layers F.Cu B.Cu) (net 2))
+  (segment (start 163 25) (end 162 25) (width 0.25) (layer B.Cu) (net 2))
+  (via (at 162 25) (size 0.6) (drill 0.4) (layers F.Cu B.Cu) (net 2))
+  (segment (start 162 25) (end 161 25) (width 0.25) (layer F.Cu) (net 2))
+  (via (at 161 25) (size 0.6) (drill 0.4) (layers F.Cu B.Cu) (net 2))
+  (segment (start 161 25) (end 160 25) (width 0.25) (layer B.Cu) (net 2))
+  (via (at 160 25) (size 0.6) (drill 0.4) (layers F.Cu B.Cu) (net 2))
+  (segment (start 160 25) (end 159 25) (width 0.25) (layer F.Cu) (net 2))
+  (via (at 159 25) (size 0.6) (drill 0.4) (layers F.Cu B.Cu) (net 2))
+  (segment (start 159 25) (end 158 25) (width 0.25) (layer B.Cu) (net 2))
+  (via (at 158 25) (size 0.6) (drill 0.4) (layers F.Cu B.Cu) (net 2))
+  (segment (start 158 25) (end 157 25) (width 0.25) (layer F.Cu) (net 2))
+  (via (at 157 25) (size 0.6) (drill 0.4) (layers F.Cu B.Cu) (net 2))
   (segment (start 137 47) (end 135.5 47) (width 0.25) (layer F.Cu) (net 2))
   (segment (start 135.5 47) (end 135 46.5) (width 0.25) (layer F.Cu) (net 2))
